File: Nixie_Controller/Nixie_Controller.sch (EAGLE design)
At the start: 69 parts, among them IC1 4028N, T1 MMBTA42, T10 MMBTA42, T11 MMBTA42, T12 MMBTA42, T13 MMBTA42, T14 MMBTA42, T15 MMBTA42, T16 MMBTA42, T17 MMBTA42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

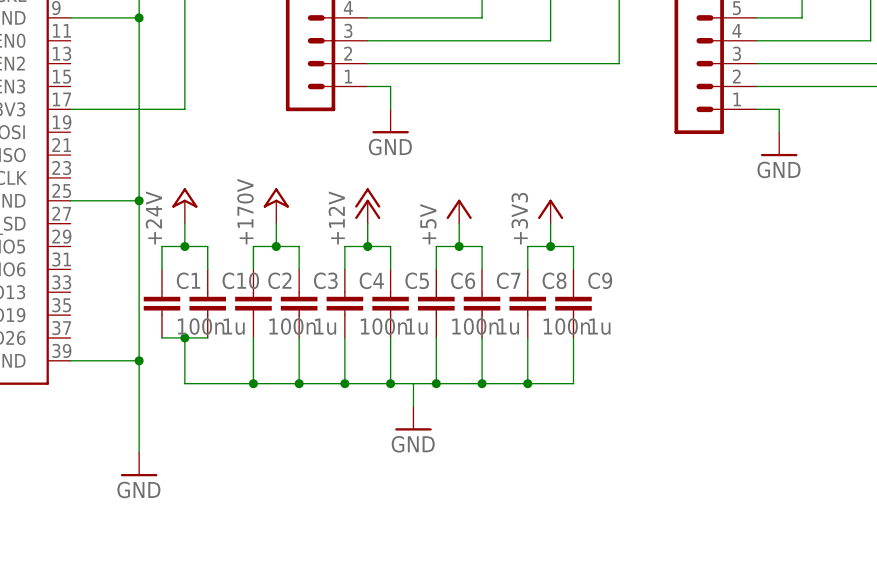
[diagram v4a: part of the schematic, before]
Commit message: fix: Reroute traces
Reroute multiple traces for a cleaner look.
Increase the tracewidth of the USB VBUS Signal.
Add decoupling capacitors to the USB supply.
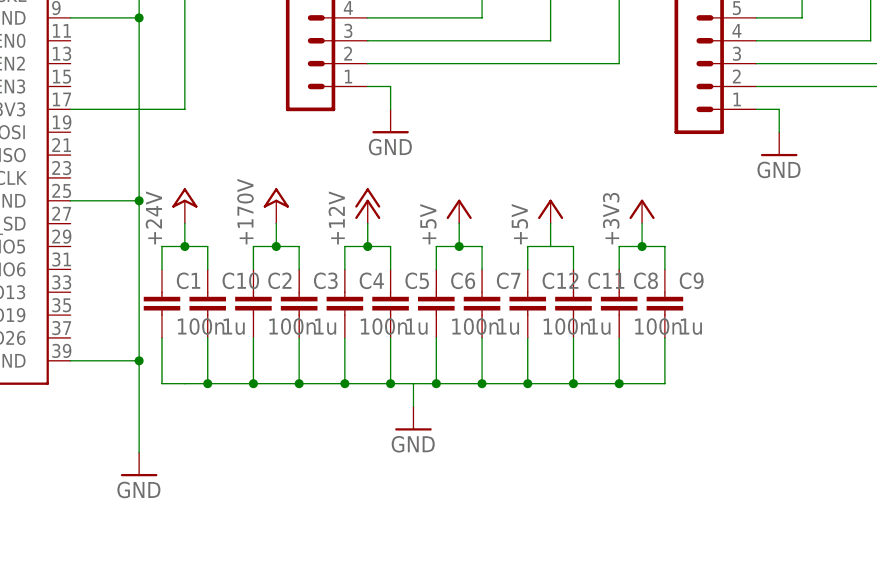
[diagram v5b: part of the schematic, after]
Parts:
- added C11: 1u, resistor:C-EUC0805
- added C12: 100n, resistor:C-EUC0805
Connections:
- net GND: now also C11.2, C12.2
- net VDD: now also C11.1, C12.1
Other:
- moved on the sheet: C8, C9
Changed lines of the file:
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@@
 <setting verticaltext="up"/>
 </settings>
-<grid distance="0.1" unitdist="inch" unit="inch" style="lines" multiple="1" display="no" altdistance="0.01" altunitdist="inch" altunit="inch"/>
+<grid distance="0.1" unitdist="inch" unit="mm" style="lines" multiple="1" display="no" altdistance="0.01" altunitdist="inch" altunit="inch"/>
 <layers>
 <layer number="1" name="Top" color="4" fill="1" visible="no" active="no"/>
@@
 <part name="T17" library="transistor" deviceset="BC850" device="" value="MMBTA42"/>
 <part name="T18" library="transistor" deviceset="BC850" device="" value="MMBTA42"/>
+<part name="P+19" library="supply1" deviceset="+5V" device=""/>
+<part name="C11" library="resistor" deviceset="C-EU" device="C0805" value="1u"/>
+<part name="C12" library="resistor" deviceset="C-EU" device="C0805" value="100n"/>
 </parts>
 <sheets>
@@
 <instance part="C6" gate="G$1" x="137.16" y="121.92"/>
 <instance part="C7" gate="G$1" x="142.24" y="121.92"/>
-<instance part="C8" gate="G$1" x="147.32" y="121.92"/>
-<instance part="C9" gate="G$1" x="152.4" y="121.92"/>
-<instance part="+3V3" gate="G$1" x="149.86" y="132.08"/>
+<instance part="C8" gate="G$1" x="157.48" y="121.92"/>
+<instance part="C9" gate="G$1" x="162.56" y="121.92"/>
+<instance part="+3V3" gate="G$1" x="160.02" y="132.08"/>
 <instance part="P+9" gate="1" x="139.7" y="132.08"/>
 <instance part="P+10" gate="1" x="129.54" y="132.08"/>
@@
 <instance part="T17" gate="G$1" x="259.08" y="391.16"/>
 <instance part="T18" gate="G$1" x="266.7" y="378.46"/>
+<instance part="P+19" gate="1" x="149.86" y="132.08"/>
+<instance part="C11" gate="G$1" x="152.4" y="121.92"/>
+<instance part="C12" gate="G$1" x="147.32" y="121.92"/>
 </instances>
 <busses>
@@
 <wire x1="142.24" y1="111.76" x2="147.32" y2="111.76" width="0.1524" layer="91"/>
 <wire x1="147.32" y1="111.76" x2="152.4" y2="111.76" width="0.1524" layer="91"/>
-<wire x1="152.4" y1="111.76" x2="152.4" y2="116.84" width="0.1524" layer="91"/>
+<wire x1="152.4" y1="111.76" x2="157.48" y2="111.76" width="0.1524" layer="91"/>
+<wire x1="157.48" y1="111.76" x2="162.56" y2="111.76" width="0.1524" layer="91"/>
+<wire x1="162.56" y1="111.76" x2="162.56" y2="116.84" width="0.1524" layer="91"/>
 <pinref part="C8" gate="G$1" pin="2"/>
-<wire x1="147.32" y1="116.84" x2="147.32" y2="111.76" width="0.1524" layer="91"/>
+<wire x1="157.48" y1="116.84" x2="157.48" y2="111.76" width="0.1524" layer="91"/>
 <pinref part="C7" gate="G$1" pin="2"/>
 <wire x1="142.24" y1="116.84" x2="142.24" y2="111.76" width="0.1524" layer="91"/>
@@
 <pinref part="C3" gate="G$1" pin="2"/>
 <wire x1="121.92" y1="116.84" x2="121.92" y2="111.76" width="0.1524" layer="91"/>
-<junction x="147.32" y="111.76"/>
+<junction x="157.48" y="111.76"/>
 <junction x="142.24" y="111.76"/>
 <junction x="137.16" y="111.76"/>
@@
 <junction x="127" y="111.76"/>
 <junction x="121.92" y="111.76"/>
+<wire x1="106.68" y1="111.76" x2="109.22" y2="111.76" width="0.1524" layer="91"/>
+<junction x="116.84" y="111.76"/>
+<pinref part="C12" gate="G$1" pin="2"/>
+<wire x1="111.76" y1="111.76" x2="116.84" y2="111.76" width="0.1524" layer="91"/>
+<wire x1="147.32" y1="116.84" x2="147.32" y2="111.76" width="0.1524" layer="91"/>
+<pinref part="C11" gate="G$1" pin="2"/>
+<wire x1="152.4" y1="116.84" x2="152.4" y2="111.76" width="0.1524" layer="91"/>
 <pinref part="C1" gate="G$1" pin="2"/>
+<wire x1="106.68" y1="116.84" x2="106.68" y2="111.76" width="0.1524" layer="91"/>
 <pinref part="C10" gate="G$1" pin="2"/>
-<wire x1="106.68" y1="116.84" x2="109.22" y2="116.84" width="0.1524" layer="91"/>
-<wire x1="109.22" y1="116.84" x2="111.76" y2="116.84" width="0.1524" layer="91"/>
-<wire x1="109.22" y1="116.84" x2="109.22" y2="111.76" width="0.1524" layer="91"/>
-<wire x1="109.22" y1="111.76" x2="116.84" y2="111.76" width="0.1524" layer="91"/>
-<junction x="116.84" y="111.76"/>
-<junction x="109.22" y="116.84"/>
+<wire x1="109.22" y1="111.76" x2="111.76" y2="111.76" width="0.1524" layer="91"/>
+<wire x1="111.76" y1="111.76" x2="111.76" y2="116.84" width="0.1524" layer="91"/>
+<junction x="111.76" y="111.76"/>
+<junction x="152.4" y="111.76"/>
+<junction x="147.32" y="111.76"/>
 </segment>
 <segment>
@@
 <segment>
 <pinref part="C8" gate="G$1" pin="1"/>
-<wire x1="147.32" y1="124.46" x2="147.32" y2="127" width="0.1524" layer="91"/>
-<wire x1="147.32" y1="127" x2="149.86" y2="127" width="0.1524" layer="91"/>
+<wire x1="157.48" y1="124.46" x2="157.48" y2="127" width="0.1524" layer="91"/>
+<wire x1="157.48" y1="127" x2="160.02" y2="127" width="0.1524" layer="91"/>
 <pinref part="C9" gate="G$1" pin="1"/>
-<wire x1="149.86" y1="127" x2="152.4" y2="127" width="0.1524" layer="91"/>
-<wire x1="152.4" y1="127" x2="152.4" y2="124.46" width="0.1524" layer="91"/>
+<wire x1="160.02" y1="127" x2="162.56" y2="127" width="0.1524" layer="91"/>
+<wire x1="162.56" y1="127" x2="162.56" y2="124.46" width="0.1524" layer="91"/>
 <pinref part="+3V3" gate="G$1" pin="+3V3"/>
-<wire x1="149.86" y1="129.54" x2="149.86" y2="127" width="0.1524" layer="91"/>
-<junction x="149.86" y="127"/>
+<wire x1="160.02" y1="129.54" x2="160.02" y2="127" width="0.1524" layer="91"/>
+<junction x="160.02" y="127"/>
 </segment>
 <segment>
@@
 <wire x1="43.18" y1="177.8" x2="43.18" y2="175.26" width="0.1524" layer="91"/>
 </segment>
-</net>
+<segment>
+<pinref part="C12" gate="G$1" pin="1"/>
+<wire x1="147.32" y1="124.46" x2="147.32" y2="127" width="0.1524" layer="91"/>
+<wire x1="147.32" y1="127" x2="149.86" y2="127" width="0.1524" layer="91"/>
+<pinref part="P+19" gate="1" pin="+5V"/>
+<wire x1="149.86" y1="127" x2="149.86" y2="129.54" width="0.1524" layer="91"/>
+<pinref part="C11" gate="G$1" pin="1"/>
+<wire x1="152.4" y1="124.46" x2="152.4" y2="127" width="0.1524" layer="91"/>
+<wire x1="152.4" y1="127" x2="149.86" y2="127" width="0.1524" layer="91"/>
+</segment>
+</net>
